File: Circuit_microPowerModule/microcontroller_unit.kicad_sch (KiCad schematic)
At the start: 34 parts, among them J1 USB_C_Receptacle_USB2.0, J5 Debug, SW2 KMR2, SW3 KMR2, U6 RP2040, U9 W25Q128JVS, Y1 12MHz

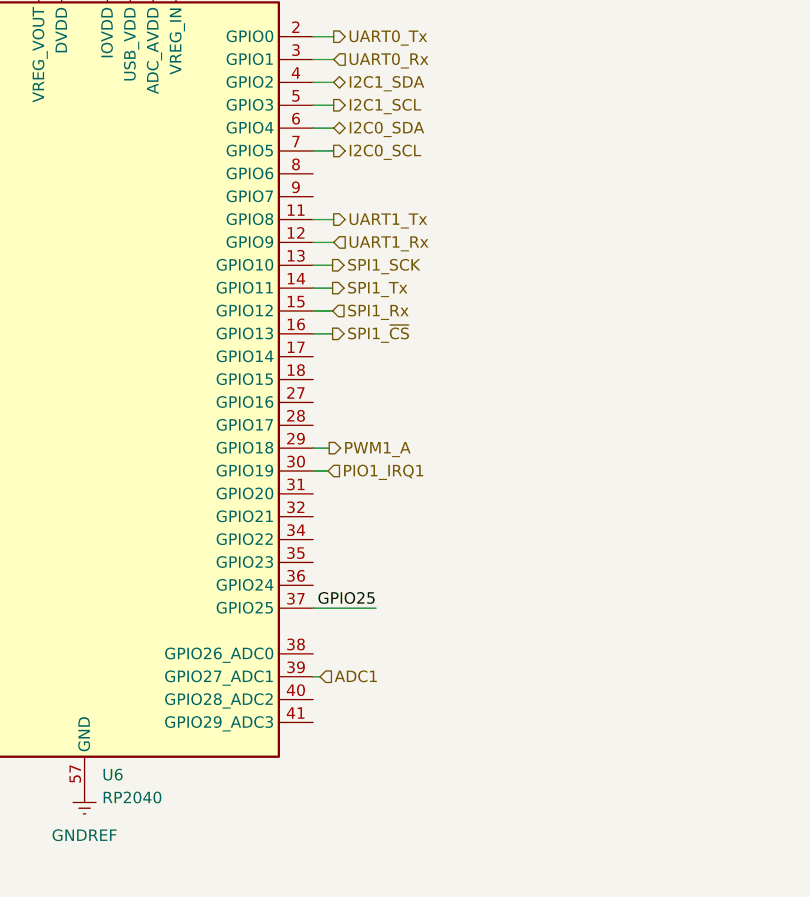
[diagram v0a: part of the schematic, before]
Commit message: Completed microcontroller unit pin planning
update schematic
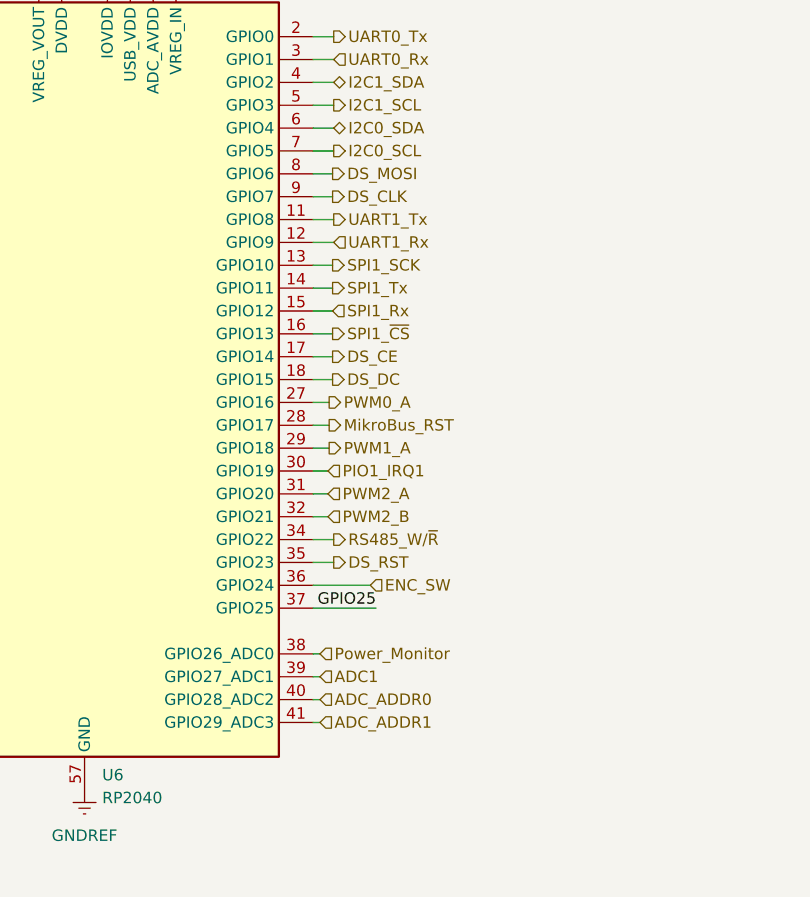
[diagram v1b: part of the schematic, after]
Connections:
- net DS_CE: now reaches U6.17 (GPIO14)
- net DS_DC: now reaches U6.18 (GPIO15)
- net PWM0_A: now reaches U6.27 (GPIO16)
- net MikroBus_RST: now reaches U6.28 (GPIO17)
- net PWM2_A: now reaches U6.31 (GPIO20)
- net PWM2_B: now reaches U6.32 (GPIO21)
- net RS485_W/~{R}: now reaches U6.34 (GPIO22)
- net DS_RST: now reaches U6.35 (GPIO23)
- net ENC_SW: now reaches U6.36 (GPIO24)
- net Power_Monitor: now reaches U6.38 (GPIO26_ADC0)
- net ADC_ADDR0: now reaches U6.40 (GPIO28_ADC2)
- net ADC_ADDR1: now reaches U6.41 (GPIO29_ADC3)
- net DS_MOSI: now reaches U6.8 (GPIO6)
- net DS_CLK: now reaches U6.9 (GPIO7)

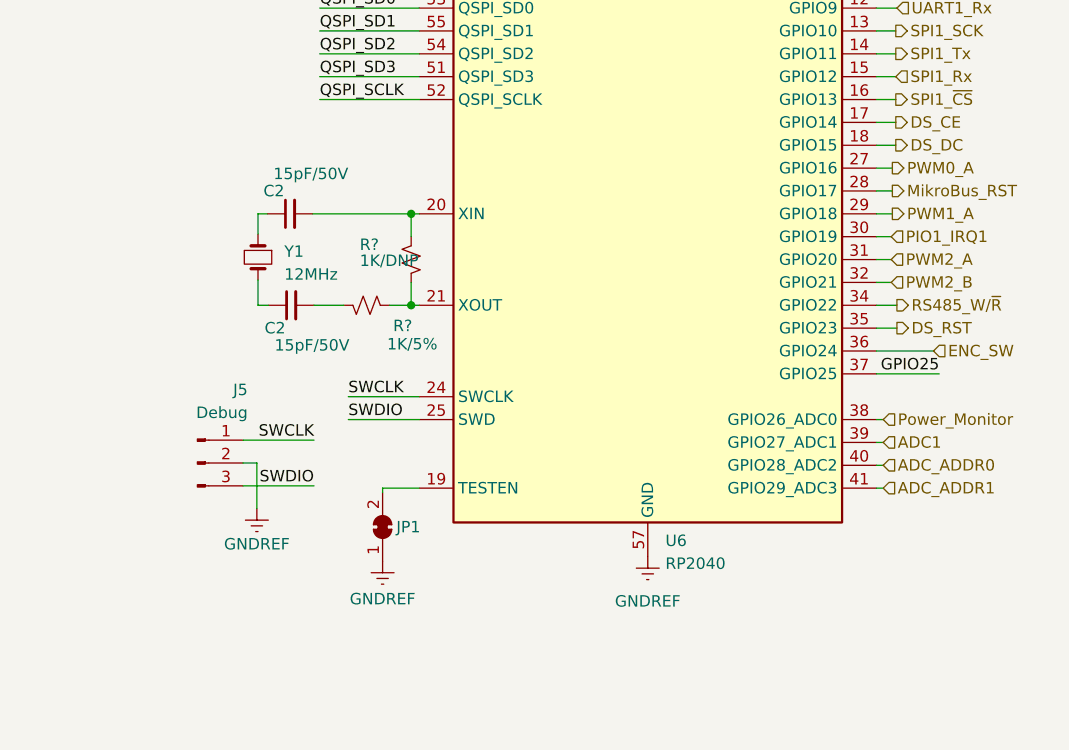
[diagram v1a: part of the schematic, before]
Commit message: change licenses
updated some footprint, create nokia 5110 lcd module pcb symbol, updated reademe
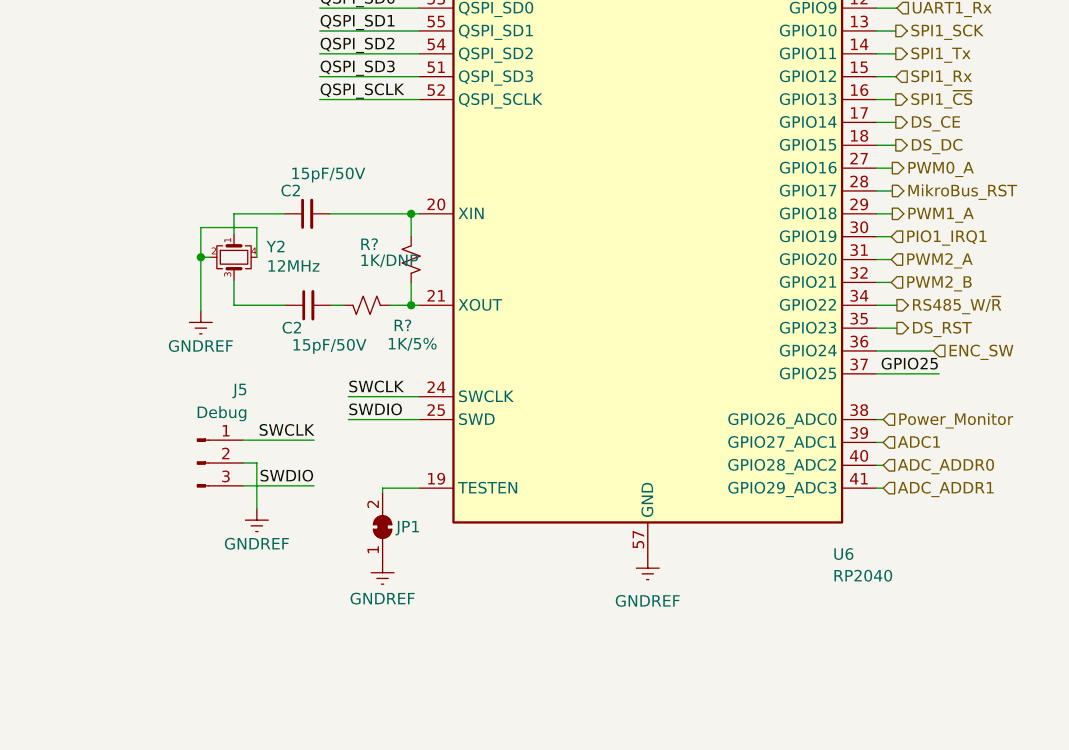
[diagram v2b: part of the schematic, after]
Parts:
- removed Y1: 12MHz, symbol Device:Crystal_Small
- added Y2: 12MHz, symbol Device:Crystal_GND24_Small
- C2: footprint (none) -> Capacitor_SMD:C_0603_1608Metric
- J5: footprint (none) -> Connector_PinHeader_2.54mm:PinHeader_1x03_P2.54mm_Vertical
- TP1, TP2, TP3: footprint (none) -> TestPoint:TestPoint_Keystone_5015_Micro-Minature
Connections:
- net GNDREF: now also Y2.2, Y2.4
- net at C2.1: now also Y2.1
- net at C2.1: now also Y2.3
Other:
- moved on the sheet: C2

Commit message: update components footprint
check boost VR component, added Nokia 5110 LCD 3D module
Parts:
- C2: footprint (none) -> Capacitor_SMD:C_0603_1608Metric
- SW2, SW3: footprint (none) -> Button_Switch_SMD:SW_Push_1P1T_NO_CK_KMR2
- Y2: footprint (none) -> Crystal:Crystal_SMD_SeikoEpson_FA238V-4Pin_3.2x2.5mm_HandSoldering
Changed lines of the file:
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@@
       (effects (font (size 1.27 1.27)) (justify left))
     )
-    (property "Footprint" "" (at 132.715 106.934 0)
+    (property "Footprint" "Capacitor_SMD:C_0603_1608Metric" (at 132.715 106.934 0)
       (effects (font (size 1.27 1.27)) hide)
     )
@@
       (effects (font (size 1.27 1.27)) (justify left))
     )
-    (property "Footprint" "" (at 39.37 105.664 0)
+    (property "Footprint" "Capacitor_SMD:C_0603_1608Metric" (at 39.37 105.664 0)
       (effects (font (size 1.27 1.27)) hide)
     )
@@
       (effects (font (size 1.27 1.27)) (justify right))
     )
-    (property "Footprint" "" (at 254.508 29.337 0)
+    (property "Footprint" "Button_Switch_SMD:SW_Push_1P1T_NO_CK_KMR2" (at 254.508 29.337 0)
       (effects (font (size 1.27 1.27)) hide)
     )
@@
       (effects (font (size 1.27 1.27)) (justify left))
     )
-    (property "Footprint" "" (at 132.588 96.774 0)
+    (property "Footprint" "Capacitor_SMD:C_0603_1608Metric" (at 132.588 96.774 0)
       (effects (font (size 1.27 1.27)) hide)
     )
@@
       (effects (font (size 1.27 1.27)) (justify right))
     )
-    (property "Footprint" "" (at 240.665 29.21 0)
+    (property "Footprint" "Button_Switch_SMD:SW_Push_1P1T_NO_CK_KMR2" (at 240.665 29.21 0)
       (effects (font (size 1.27 1.27)) hide)
     )
@@
       (effects (font (size 1.27 1.27)))
     )
-    (property "Footprint" "" (at 124.46 101.6 0)
+    (property "Footprint" "Crystal:Crystal_SMD_SeikoEpson_FA238V-4Pin_3.2x2.5mm_HandSoldering" (at 124.46 101.6 0)
       (effects (font (size 1.27 1.27)) hide)
     )
@@
       (effects (font (size 1.27 1.27)) (justify left))
     )
-    (property "Footprint" "" (at 207.01 27.94 0)
-      (effects (font (size 1.27 1.27)) hide)
-    )
+    (property "Footprint" "Capacitor_SMD:C_0603_1608Metric" (at 207.01 27.94 0)
+      (effects (font (size 1.27 1.27)) hide)
+    )

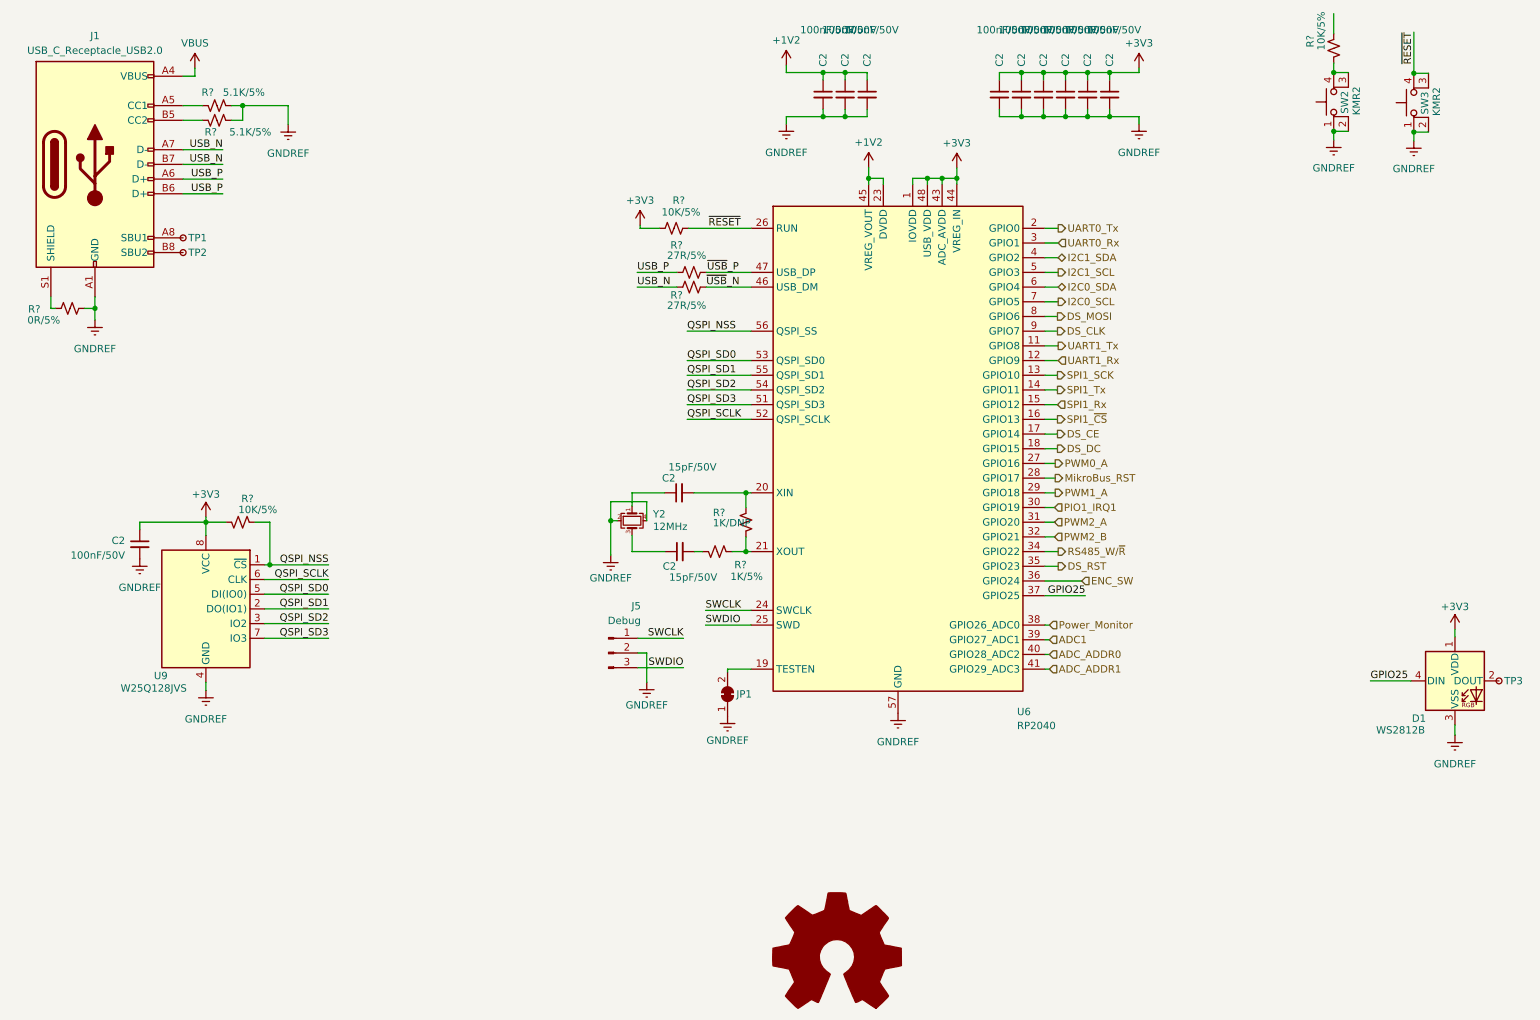
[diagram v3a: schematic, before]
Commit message: update schematic
added pin assessment to readme
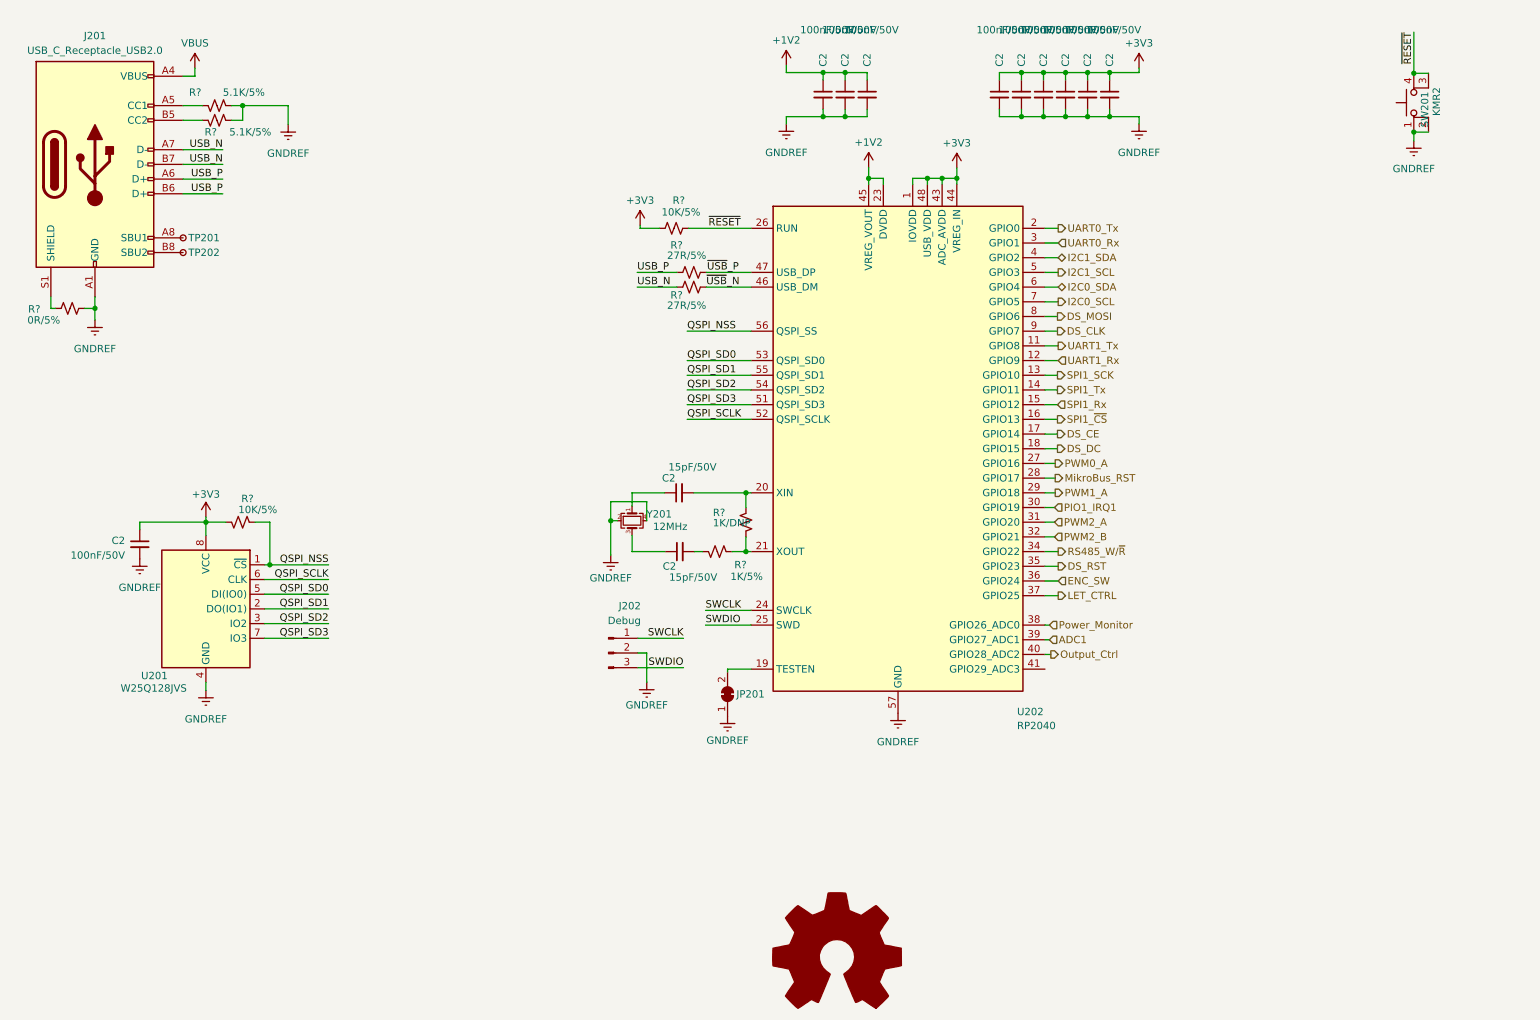
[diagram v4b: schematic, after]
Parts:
- removed D1: WS2812B, LED_SMD:LED_WS2812B_PLCC4_5.0x5.0mm_P3.2mm, symbol LED:WS2812B
- removed R?: 10K/5%, Resistor_SMD:R_0603_1608Metric, symbol Device:R_Small_US
- removed SW2: KMR2, Button_Switch_SMD:SW_Push_1P1T_NO_CK_KMR2, symbol Switch:SW_MEC_5E
- removed TP3: TestPoint_Small, TestPoint:TestPoint_Keystone_5015_Micro-Minature, symbol Connector:TestPoint_Small
- renumbered J1 to J201, J5 to J202, JP1 to JP201, SW3 to SW201, TP1 to TP201, TP2 to TP202, U9 to U201, U6 to U202, Y2 to Y201
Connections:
- net ADC_ADDR0 renamed Output_Ctrl
- net ADC_ADDR1: no longer names the net of U202.41 (GPIO29_ADC3)
- net GPIO25 renamed LET_CTRL
